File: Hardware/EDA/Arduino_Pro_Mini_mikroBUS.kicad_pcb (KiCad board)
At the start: 4 copper layers, 38.1 x 69.8 mm, 36 parts, among them CON1 BARREL_JACK, J1 HEADER_F_2.54MM_1R8P_ST_AU_PTH, J2 HEADER_F_2.54MM_1R8P_ST_AU_PTH, J3 HEADER_F_2.54MM_1R12P_ST_AU_P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, J4 HEADER_F_2.54MM_1R12P_ST_AU_P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, J5 Molex_0475710001, J6 HEADER_F_2.54MM_1R2P_ST_AU_PTH, M1 FID, M2 FID, M3 FID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

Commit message: Changed uSD CS pin to D10. Connected mikroBUS PWM pin to D6. Altered front silkscreen. Generated PDF schematic and Gerbers.
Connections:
- J2 pad 1: (no net) -> D6
- J3 pad 1: (no net) -> D10
- J5 pad 2: D6 -> D10
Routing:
- net D10: track 0.00 -> 17.5 mm, vias 0 -> 1
- net D6: track 28.0 -> 34.6 mm, vias 1 -> 0
- net D5: track 44.5 -> 45.2 mm
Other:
- board text added: "microSD"
- board text added: "mikroBUS"
- board text removed: "mikroBUS Socket"
- board text removed: "uSD"

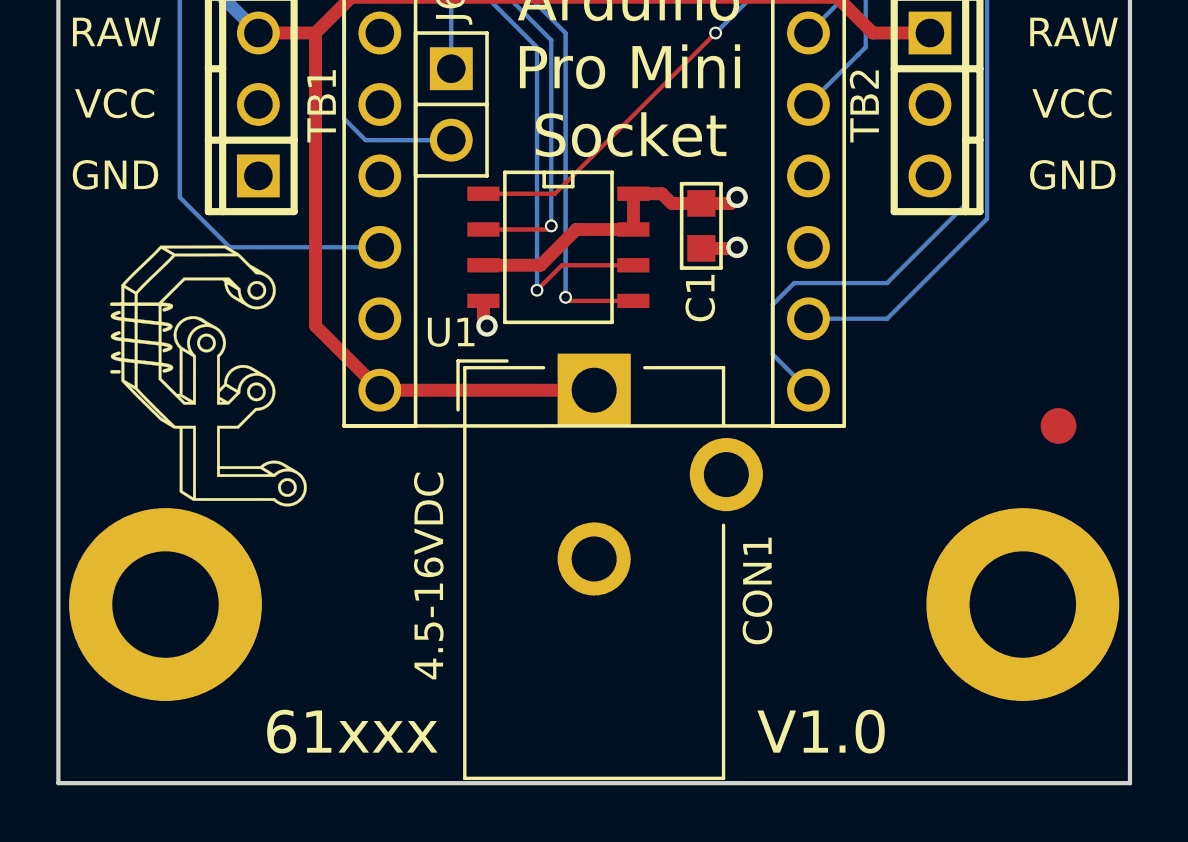
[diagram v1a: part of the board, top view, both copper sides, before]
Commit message: Updated silkscreen artwork. Generated new gerbers and BOM.
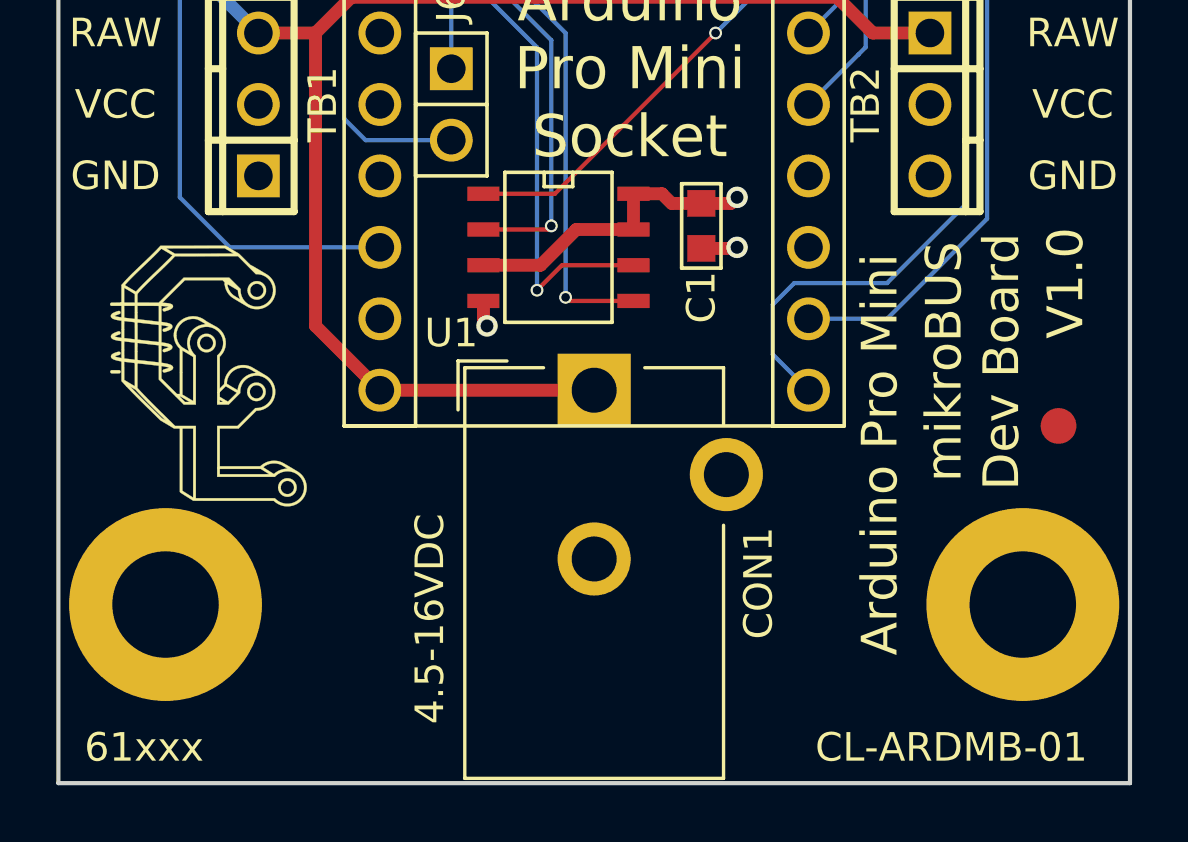
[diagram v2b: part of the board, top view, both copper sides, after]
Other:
- board text added: "Arduino Pro Mini"
- board text added: "CL-ARDMB-01"
- board text added: "mikroBUS Dev Board"
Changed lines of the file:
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@@
     (area 60.884999 31.674999 99.135001 101.675001)
     (thickness 1.6)
-    (drawings 34)
+    (drawings 37)
     (tracks 319)
     (zones 0)
@@
       (drillshape 0)
       (scaleselection 1)
-      (outputdirectory Z:/Engineering/Projects/Adapter_Boards/Arduino_Pro_Mini_mikroBUS/Hardware/EDA/Gerbers/))
+      (outputdirectory Gerbers/))
   )
   (net 0 "")
@@
     (descr "Thin-pin DC Barrel Jack, https://cdn-shop.adafruit.com/datasheets/21mmdcjackDatasheet.pdf")
     (tags "Power Jack")
-    (fp_text reference CON1 (at 5.842 7.112 90) (layer F.SilkS)
+    (fp_text reference CON1 (at 5.842 6.858 90) (layer F.SilkS)
       (effects (font (size 1.016 1.016) (thickness 0.1524)))
     )
@@
       (net 2 GND))
   )
+  (gr_text CL-ARDMB-01 (at 92.71 100.33) (layer F.SilkS)
+    (effects (font (size 1.016 1.016) (thickness 0.2032)))
+  )
+  (gr_text "mikroBUS\nDev Board" (at 93.472 86.614 90) (layer F.SilkS)
+    (effects (font (size 1.27 1.27) (thickness 0.254)))
+  )
+  (gr_text "Arduino Pro Mini" (at 90.17 89.916 90) (layer F.SilkS)
+    (effects (font (size 1.27 1.27) (thickness 0.254)))
+  )
   (dimension 30.48 (width 0.3) (layer Dwgs.User)
     (gr_text "1.2000 in" (at 80.01 108.03) (layer Dwgs.User)
@@
     (arrow2b (pts (xy 57.15 101.6) (xy 56.563579 100.473496)))
   )
-  (gr_text 61xxx (at 71.374 99.822) (layer F.SilkS)
-    (effects (font (size 1.5 1.5) (thickness 0.3)))
-  )
-  (gr_text V1.0 (at 88.138 99.822) (layer F.SilkS)
-    (effects (font (size 1.5 1.5) (thickness 0.3)))
+  (gr_text 61xxx (at 64.008 100.33) (layer F.SilkS)
+    (effects (font (size 1.016 1.016) (thickness 0.2032)))
+  )
+  (gr_text V1.0 (at 96.774 83.82 90) (layer F.SilkS)
+    (effects (font (size 1.27 1.27) (thickness 0.254)))
   )
   (gr_text microSD (at 80.264 39.116) (layer F.SilkS)
     (effects (font (size 1.5 1.5) (thickness 0.3)))
   )
-  (gr_text 4.5-16VDC (at 74.168 94.234 90) (layer F.SilkS)
+  (gr_text 4.5-16VDC (at 74.168 95.758 90) (layer F.SilkS)
     (effects (font (size 1.016 1.016) (thickness 0.2032)))
   )
@@
   (segment (start 88.9 71.628) (end 88.392 71.12) (width 0.1524) (layer B.Cu) (net 18))
   (segment (start 88.9 73.66) (end 88.9 71.628) (width 0.1524) (layer B.Cu) (net 18))
-  (segment (start 87.63 67.31) (end 89.154 65.786) (width 0.1524) (layer B.Cu) (net 19) (status 400000))
-  (segment (start 89.154 36.576) (end 91.44 34.29) (width 0.1524) (layer B.Cu) (net 19) (status 800000))
+  (segment (start 87.63 67.31) (end 89.154 65.786) (width 0.1524) (layer B.Cu) (net 19))
+  (segment (start 89.154 36.576) (end 91.44 34.29) (width 0.1524) (layer B.Cu) (net 19))
   (segment (start 89.154 65.786) (end 89.154 36.576) (width 0.1524) (layer B.Cu) (net 19))
   (segment (start 82.677 63.373) (end 82.423 63.373) (width 0.1524) (layer F.Cu) (net 20))

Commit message: Corrected part# on silkscreen artwork.
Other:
- board text added: "61539"
- board text removed: "61xxx"
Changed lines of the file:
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@@
     (links 93)
     (no_connects 1)
-    (area 60.884999 31.674999 99.135001 101.675001)
+    (area 45.184287 23.97 111.025715 109.380001)
     (thickness 1.6)
     (drawings 37)
@@
     (arrow2b (pts (xy 57.15 101.6) (xy 56.563579 100.473496)))
   )
-  (gr_text 61xxx (at 64.008 100.33) (layer F.SilkS)
+  (gr_text 61539 (at 64.008 100.33) (layer F.SilkS)
     (effects (font (size 1.016 1.016) (thickness 0.2032)))
   )
